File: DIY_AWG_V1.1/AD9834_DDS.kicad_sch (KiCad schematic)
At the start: 65 parts, among them IC1 ADG704BRMZ-REEL7, IC2 TLV3544IPWR, U11 AD9834, U12 OPA171AIDRLR, Y2 SG-615

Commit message: Updated STM32_MCU, amplifier, User_Interface, AD9834_DDS schematic
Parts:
- removed C50, C52: 10u, symbol Device:C_Polarized
- removed C59: 0.1u, symbol Device:C
- removed R34: 300, symbol Device:R
- removed Y2: SG-615, Oscillator:Oscillator_SMD_SeikoEpson_SG8002JA-4Pin_14.0x8.7mm, symbol Oscillator:SG-615
- added C47: 100n, symbol Device:C
- added C56, C62, C65, C66, C71, C72: 10u, symbol Device:C
- added U11: 8121H-50.000NK33DRL, easyeda2kicad:OSC-SMD_4P-L2.0-W1.6-BL_SIT8008BI-72-33E-54.000000, symbol easyeda2kicad:8121H-50.000NK33DRL
- C55: renamed from C49; value 0.1u -> 100n
- C59: renamed from C46; value 0.1uF -> 100n
- C61: renamed from C51; value 0.1u -> 100n
- C67: renamed from C53; value 6.8u -> 10u
- C68: renamed from C54; value 0.1uF -> 100n
- C69: renamed from C55; value 0.1uF -> 100n
- C70: renamed from C56; value 6.8u -> 10u
- R21: renamed from R27; value 10 -> 9.53
- renumbered C35 to C44, C36 to C45, C37 to C46, C38 to C48, C39 to C49, C40 to C50, C41 to C51, C48 to C52, C42 to C53, C43 to C54, C44 to C57, C45 to C58, C47 to C60, C57 to C63, C58 to C64, L11 to L10, L8 to L7, L9 to L8, L10 to L9, R20 to R14, R21 to R15, R22 to R16, R23 to R17, R24 to R18, R25 to R19, R26 to R20, R35 to R22, R36 to R23, R28 to R24, R29 to R25, R30 to R26, R31 to R27, R32 to R28, R33 to R29, TP13 to TP10, TP14 to TP11, TP15 to TP12, TP16 to TP13, TP17 to TP14, TP18 to TP15, TP19 to TP16, TP8 to TP17, TP20 to TP18, TP9 to TP19, TP10 to TP20, TP11 to TP21, TP12 to TP22, TP21 to TP23, U11 to U12, U12 to U13
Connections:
- net +3.3VA: now also C62.1
- net +5.0VA: now also C65.1, C66.1
- net -5.0VA: now also C71.1, C72.1
- net GND: now also C47.2, C56.1, C62.2, C65.2, C66.2, C71.2, C72.2, U11.2 (GND)
- net WAVE2_OUT: now also U12.17 (VIN)
- net at TP10.1, U12.8 (MCLK): now also U11.3 (OUT)
- net +3.3VD renamed +3V3
- net +3V3: now also C47.1, C56.2, U11.4 (VCC)
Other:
- note added: "8.2pF MLCC (1): 0402CG8R2G500NT (1) 20pF MLCC (1): TCC0603COG200G500CT (1) 24pF MLCC (1): TCC0603COG240G500CT (1) 39pF MLCC (1): GRM1885C2E390FW07D (1) 47pF MLCC (1): C0603C470F5GACAUTO (1) 68pF MLCC (1): CC0603GRNPO9BN680 (1) 75pF MLCC (1): CC0603GRNPO9BN750 (1) 82pF MLCC (1): GCM1885C2A820FA16D (1) 510pF MLCC (2): 0603C0G511J500NT (2) 10nF MLCC (2): TCC0603COG103J500CT (2) 100nF MLCC (8): C0603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"
- note added: "AD9834"
- note removed: "10uF Tantalum Caps"
- note removed: "8.2pF MLCC (1): 0402CG8R2G500NT (1) 20pF MLCC (1): TCC0603COG200G500CT (1) 24pF MLCC (1): TCC0603COG240G500CT (1) 39pF MLCC (1): GRM1885C2E390FW07D (1) 47pF MLCC (1): C0603C470F5GACAUTO (1) 68pF MLCC (1): CC0603GRNPO9BN680 (1) 75pF MLCC (1): CC0603GRNPO9BN750 (1) 82pF MLCC (1): GCM1885C2A820FA16D (1) 510pF MLCC (2): 0603C0G511J500NT (2) 100nF MLCC (1): C0603C104J3RACTU (1) 2.2uF MLCC (1): 0603YD2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"
- moved on the sheet: C46, C49, C52, C53, C55, C57, C59, C61, C63, C64, C67, C68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

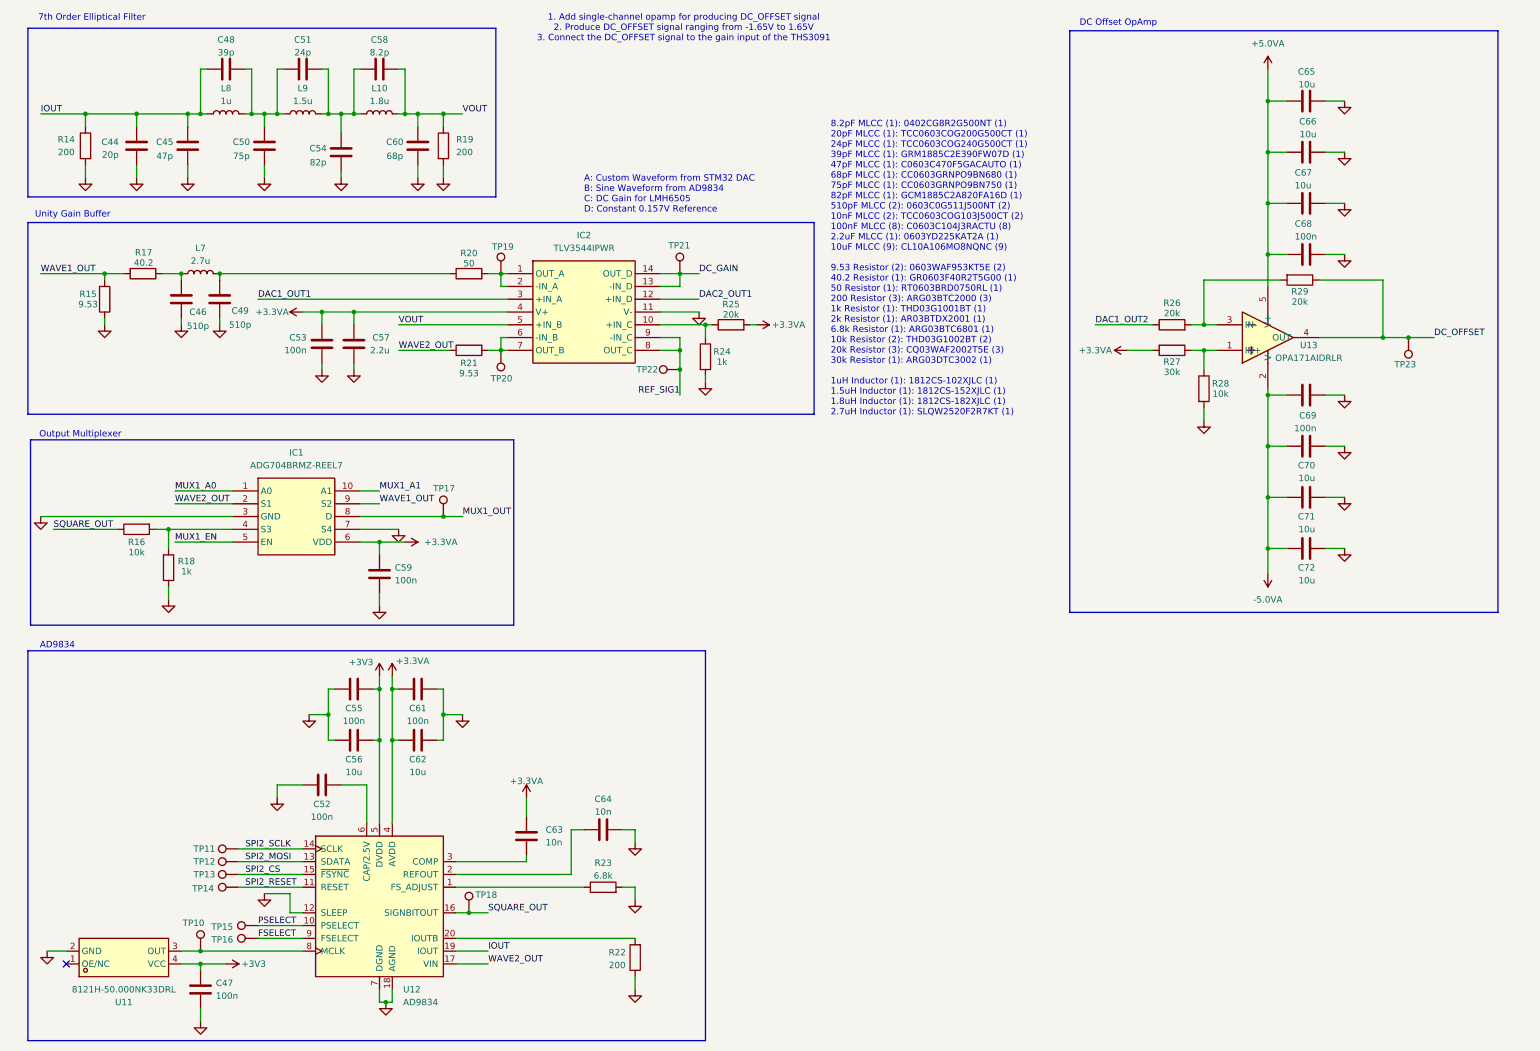
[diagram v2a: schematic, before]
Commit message: Updated pin description of relevant components
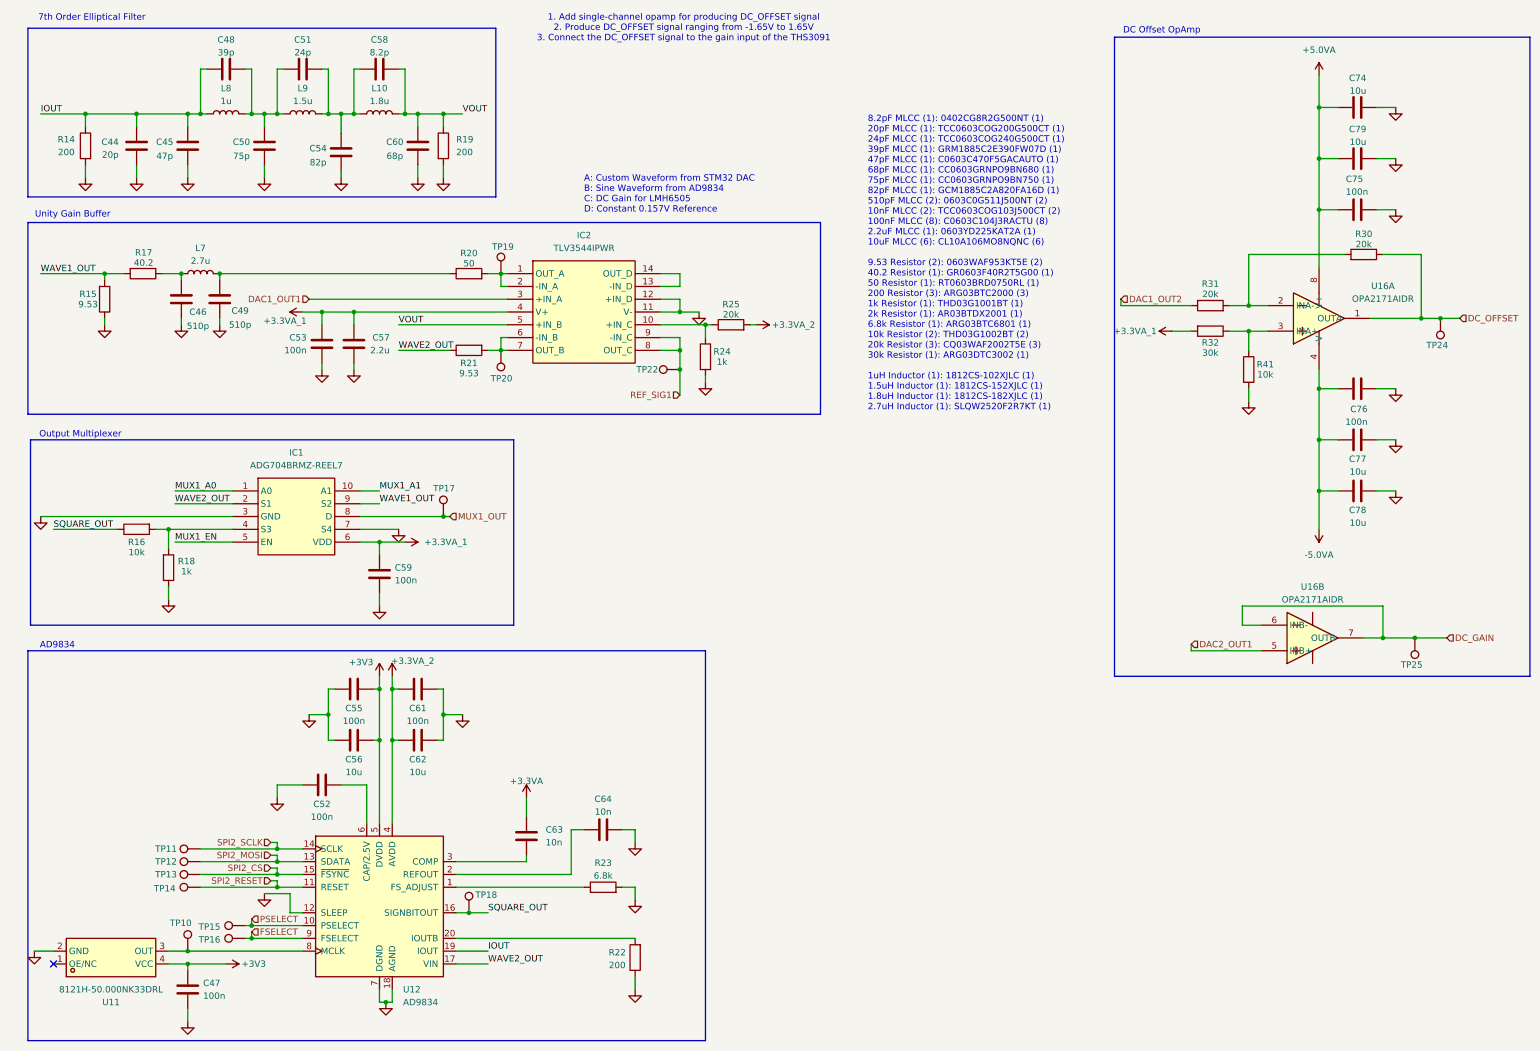
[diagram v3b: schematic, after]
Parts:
- removed C65, C66, C67, C70, C71, C72: 10u, symbol Device:C
- removed C68, C69: 100n, symbol Device:C
- removed R26, R29: 20k, symbol Device:R
- removed R27: 30k, symbol Device:R
- removed R28: 10k, symbol Device:R
- removed TP21, TP23: TestPoint, symbol Connector:TestPoint
- removed U13: OPA171AIDRLR, easyeda2kicad:SOT-5X3-5_L1.6-W1.2-P0.50-LS1.6-BR, symbol easyeda2kicad:OPA171AIDRLR
- added C74, C77, C78, C79: 10u, symbol Device:C
- added C75, C76: 100n, symbol Device:C
- added R30, R31: 20k, symbol Device:R
- added R32: 30k, symbol Device:R
- added R41: 10k, symbol Device:R
- added TP24, TP25: TestPoint, symbol Connector:TestPoint
- added U16: OPA2171AIDR, easyeda2kicad:SOIC-8_L5.0-W4.0-P1.27-LS6.0-BL, symbol easyeda2kicad:OPA2171AIDR
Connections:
- net +3.3VA: no longer C53.1, C57.1, C59.1, C61.1, C62.1, IC1.6 (VDD), IC2.4 (V+), R25.2, U12.4 (AVDD)
- net +5.0VA: now also C74.1, C75.1, C79.1, U16.8 (V+)
- net -5.0VA: now also C76.1, C77.1, C78.1, U16.4 (V-)
- net DAC1_OUT2: now also R31.1
- net DAC2_OUT1: now also U16.5 (INB+); no longer IC2.12 (+IN_D)
- net DC_GAIN: now also TP25.1, U16.6 (INB-), U16.7 (OUTB); no longer IC2.13 (-IN_D), IC2.14 (OUT_D)
- net DC_OFFSET: now also R30.1, TP24.1, U16.1 (OUTA)
- net GND: now also IC2.12 (+IN_D), C74.2, C75.2, C76.2, C77.2, C78.2, C79.2, R41.2
- new net: R30.2, R31.2, U16.2 (INA-)
- new net: R32.1, R41.1, U16.3 (INA+)
- new net: IC2.13 (-IN_D), IC2.14 (OUT_D)
- new net +3.3VA_1: C53.1, C57.1, C59.1, IC1.6 (VDD), IC2.4 (V+), R32.2
- new net +3.3VA_2: C61.1, C62.1, R25.2, U12.4 (AVDD)
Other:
- moved on the sheet: C47, TP10, TP11, TP12, TP13, TP14, TP15, TP16, U11

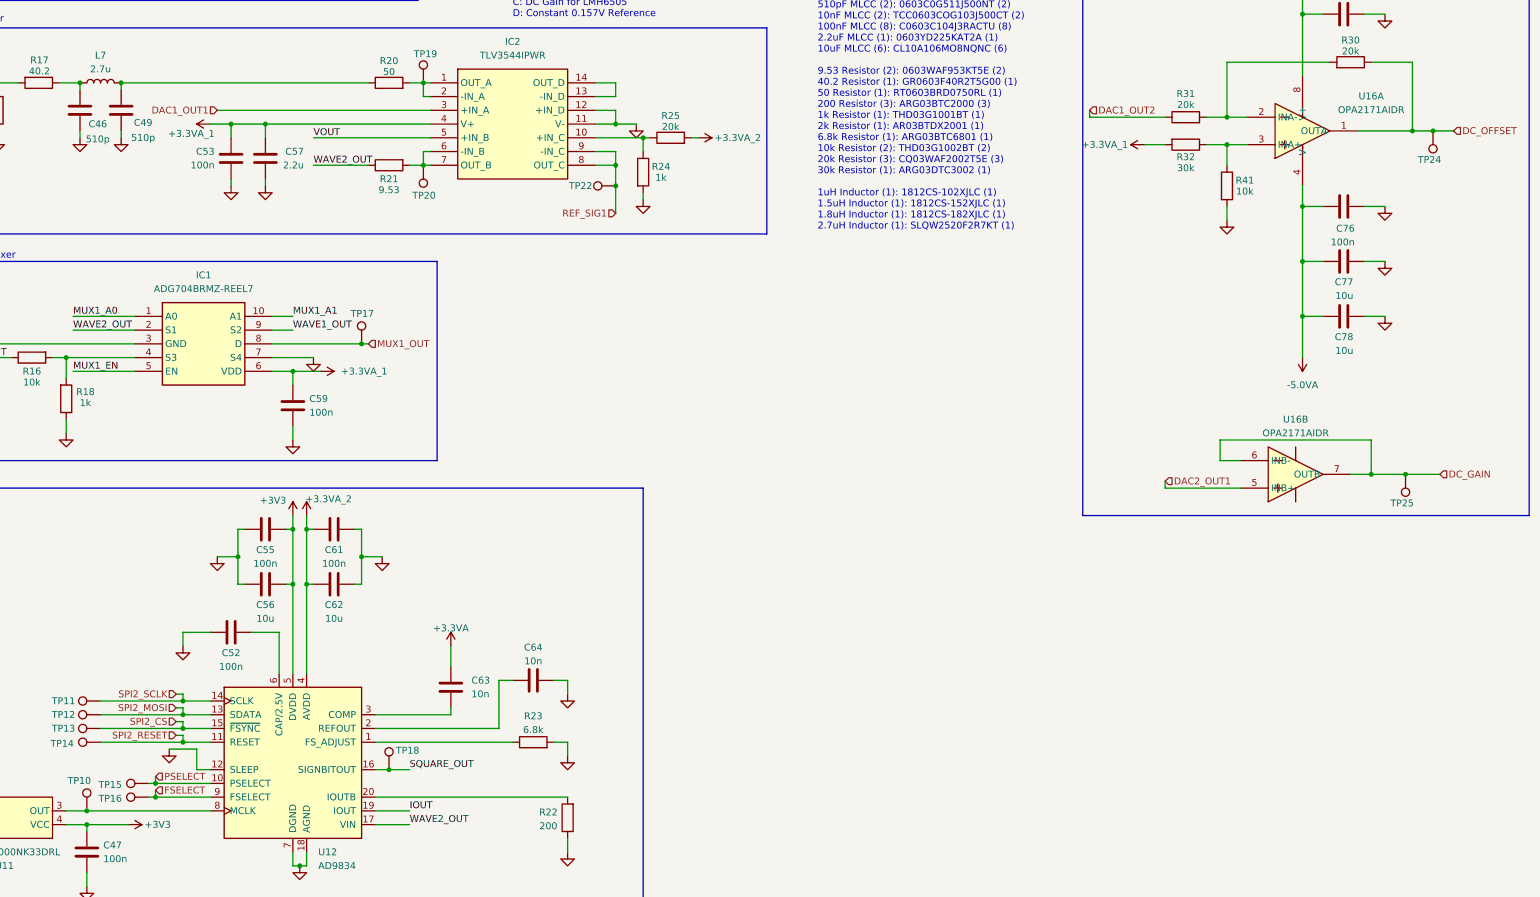
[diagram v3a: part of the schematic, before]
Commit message: Updated schematics to clear ERCs
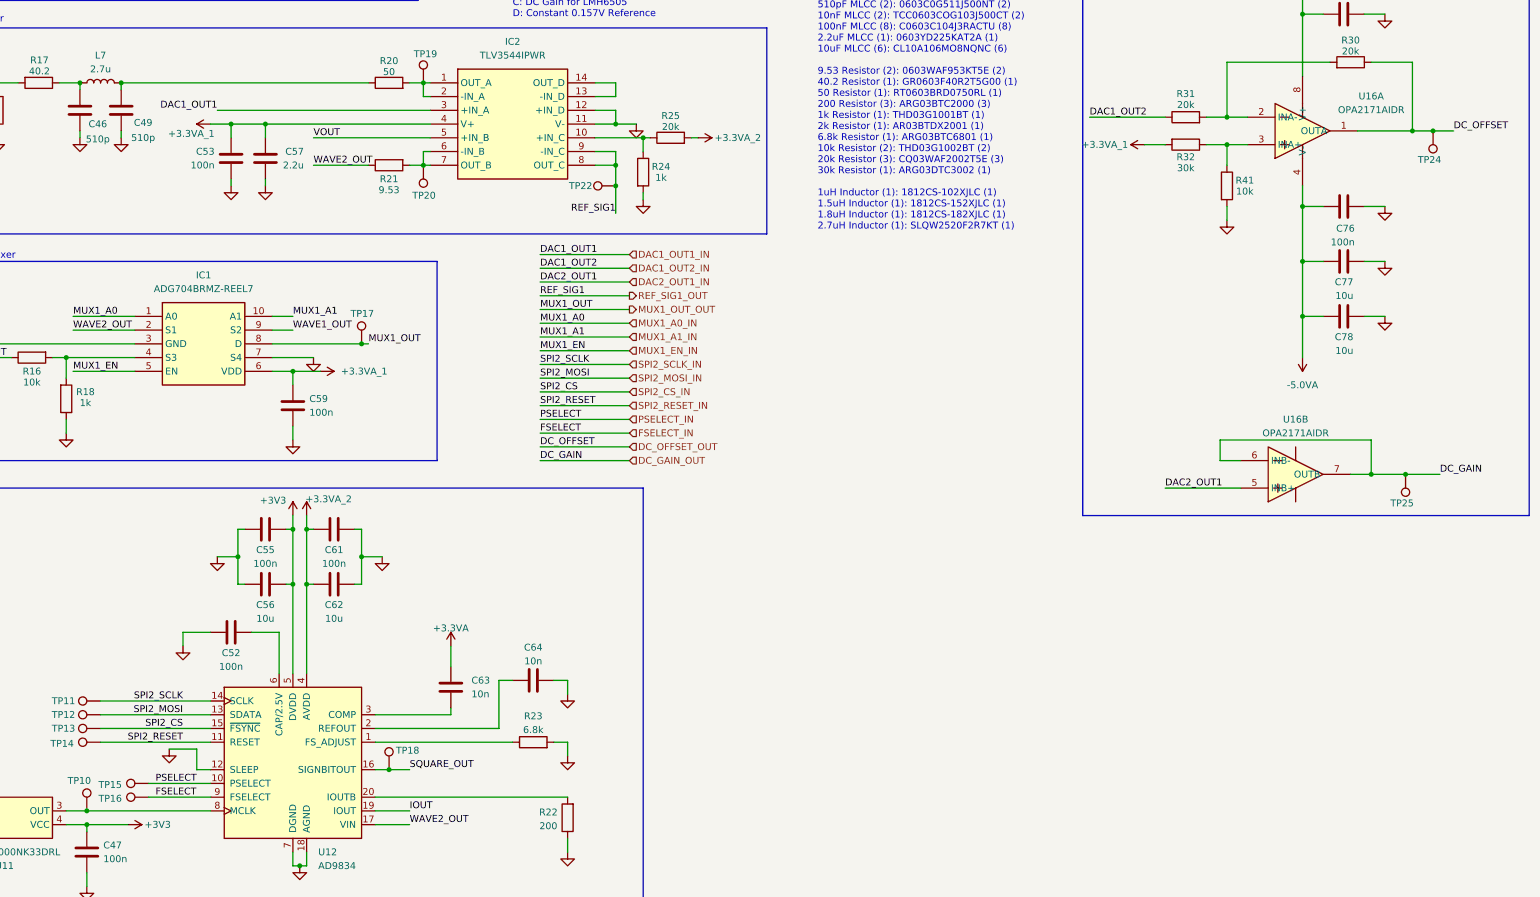
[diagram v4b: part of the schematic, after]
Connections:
- net DAC1_OUT1 renamed DAC1_OUT1_IN
- net DAC1_OUT2 renamed DAC1_OUT2_IN
- net DAC2_OUT1 renamed DAC2_OUT1_IN
- net DC_GAIN renamed DC_GAIN_OUT
- net DC_OFFSET renamed DC_OFFSET_OUT
- net FSELECT renamed FSELECT_IN
- net MUX1_A0 renamed MUX1_A0_IN
- net MUX1_A1 renamed MUX1_A1_IN
- net MUX1_EN renamed MUX1_EN_IN
- net MUX1_OUT renamed MUX1_OUT_OUT
- net PSELECT renamed PSELECT_IN
- net REF_SIG1 renamed REF_SIG1_OUT
- net SPI2_CS renamed SPI2_CS_IN
- net SPI2_MOSI renamed SPI2_MOSI_IN
- net SPI2_RESET renamed SPI2_RESET_IN
- net SPI2_SCLK renamed SPI2_SCLK_IN
